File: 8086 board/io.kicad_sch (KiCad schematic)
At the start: 108 parts, among them SW1 SW_Push, SW10 SW_Push, SW11 SW_Push, SW12 SW_Push, SW13 SW_Push, SW14 SW_Push, SW15 SW_Push, SW16 SW_Push, SW17 SW_Push, SW18 SW_Push, SW19 SW_Push, SW2 SW_Push, SW20 SW_Push, SW21 SW_Push, SW22 SW_Push, SW23 SW_Push, SW24 SW_Push, SW25 SW_Push, SW26 SW_Push, SW27 SW_Push, SW28 SW_Push, SW29 SW_Push, SW3 SW_Push, SW30 SW_Push, SW31 SW_Push, SW32 SW_Push, SW4 SW_Push, SW5 SW_Push, SW6 SW_Push, SW7 SW_Push, SW8 SW_Push, SW9 SW_Push, U16 74AC373, U28 74AC373, U30 74AC00, U31 74HC02, U32 74AC373, U33 74AC373, U34 74AC373, U35 74AC373, U36 74AC373, U37 74AC373

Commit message: refactoring schematic files and structure
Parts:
- added U15: AMS1117-3.3, Package_TO_SOT_SMD:SOT-223-3_TabPin2, symbol Regulator_Linear:AMS1117-3.3
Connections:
- net +5V: now also U15.3 (VI)
- net GND: now also U15.1 (GND)
- new net +3.3V: U15.2 (VO)

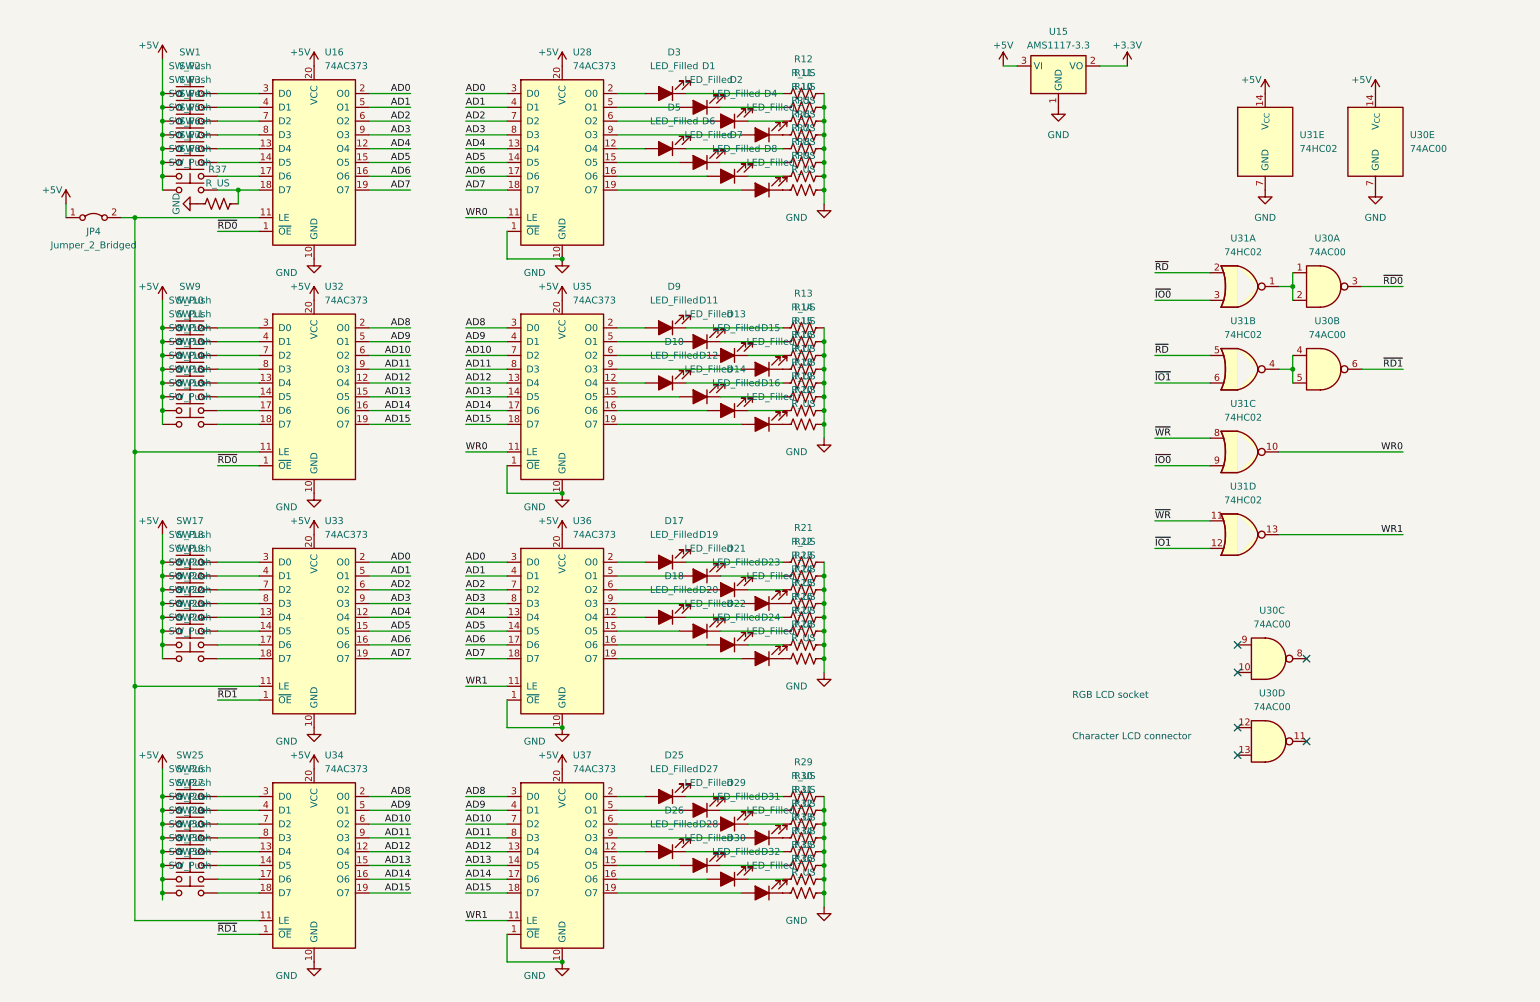
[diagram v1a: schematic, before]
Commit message: better schematic. initial pcb layout
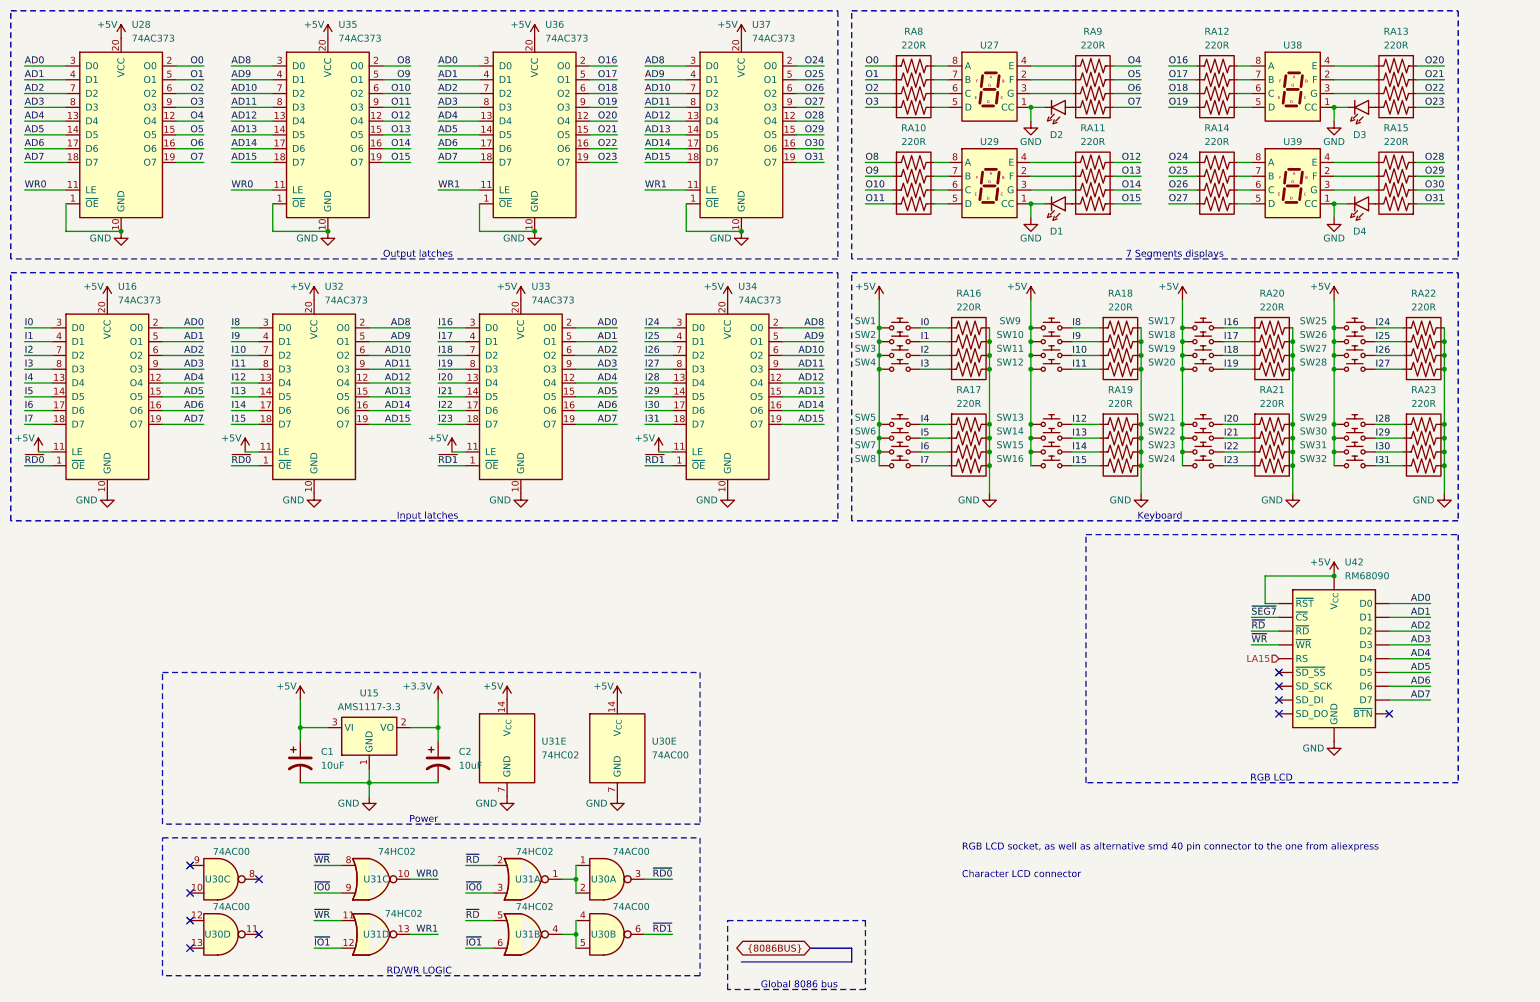
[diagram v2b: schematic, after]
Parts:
- removed D1, D10, D11, D12, D13, D14, D15, D16, D17, D18, D19, D2, D20, D21, D22, D23, D24, D25, D26, D27, D28, D29, D3, D30, D31, D32, D4, D5, D6, D7, D8, D9: LED_Filled, LED_SMD:LED_0603_1608Metric_Pad1.05x0.95mm_HandSolder, symbol Device:LED_Filled
- removed JP4: Jumper_2_Bridged, symbol Jumper:Jumper_2_Bridged
- removed R10, R11, R12, R13, R14, R15, R16, R17, R18, R19, R20, R21, R22, R23, R24, R25, R26, R27, R28, R29, R30, R31, R32, R33, R34, R35, R36, R37, R5, R6, R7, R8, R9: R_US, Resistor_SMD:R_0603_1608Metric_Pad0.98x0.95mm_HandSolder, symbol Device:R_US
- removed SW1, SW10, SW11, SW12, SW13, SW14, SW15, SW16, SW17, SW18, SW19, SW2, SW20, SW21, SW22, SW23, SW24, SW25, SW26, SW27, SW28, SW29, SW3, SW30, SW31, SW32, SW4, SW5, SW6, SW7, SW8, SW9: SW_Push, Button_Switch_SMD:SW_Push_1P1T_NO_6x6mm_H9.5mm, symbol Switch:SW_Push
- added C1, C2: 10uF, symbol Device:C_Polarized_US
- added D1, D2, D3, D4: LED, symbol 8086PC:LED
- added RA10, RA11, RA12, RA13, RA14, RA15, RA16, RA17, RA18, RA19, RA20, RA21, RA22, RA23, RA8, RA9: 220R, Resistor_SMD:R_Array_Concave_4x0603, symbol 8086PC:R_Array_4
- added SW1, SW10, SW11, SW12, SW13, SW14, SW15, SW16, SW17, SW18, SW19, SW2, SW20, SW21, SW22, SW23, SW24, SW25, SW26, SW27, SW28, SW29, SW3, SW30, SW31, SW32, SW4, SW5, SW6, SW7, SW8, SW9: ~, Button_Switch_SMD:SW_Push_1P1T_NO_6x6mm_H9.5mm, symbol 8086PC:SW_Push
- added U27, U29, U38, U39: ~, symbol 8086PC:2181AS
- added U42: RM68090, symbol 8086PC:RM68090
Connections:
- net +3.3V: now also C2.1
- net +5V: now also U16.11 (LE), U32.11 (LE), U33.11 (LE), U34.11 (LE), C1.1, SW1.1, SW10.1, SW11.1, SW12.1, SW13.1, SW14.1, SW15.1, SW16.1, SW17.1, SW18.1, SW19.1, SW2.1, SW20.1, SW21.1, SW22.1, SW23.1, SW24.1, SW25.1, SW26.1, SW27.1, SW28.1, SW29.1, SW3.1, SW30.1, SW31.1, SW32.1, SW4.1, SW5.1, SW6.1, SW7.1, SW8.1, SW9.1, U42. (~{WR})
- net AD0: now also U42. (~{WR})
- net AD1: now also U42. (~{WR})
- net AD2: now also U42. (~{WR})
- net AD3: now also U42. (~{WR})
- net AD4: now also U42. (~{WR})
- net AD5: now also U42. (~{WR})
- net AD6: now also U42. (~{WR})
- net AD7: now also U42. (~{WR})
- net GND: now also C1.2, C2.2, D1.2 (K), D2.2 (K), D3.2 (K), D4.2 (K), RA16.5, RA16.6, RA16.7, RA16.8, RA17.5, RA17.6, RA17.7, RA17.8, RA18.5, RA18.6, RA18.7, RA18.8, RA19.5, RA19.6, RA19.7, RA19.8, RA20.5, RA20.6, RA20.7, RA20.8, RA21.5, RA21.6, RA21.7, RA21.8, RA22.5, RA22.6, RA22.7, RA22.8, RA23.5, RA23.6, RA23.7, RA23.8, U27.1 (CC), U29.1 (CC), U38.1 (CC), U39.1 (CC), U42. (~{WR})
- net ~{RD}: now also U42. (~{WR})
- net ~{WR}: now also U42. (~{WR})
- net I12: now reaches U32.13 (D4)
- net I12: now also RA19.1, SW13.2
- net I13: now reaches U32.14 (D5)
- net I13: now also RA19.2, SW14.2
- net I14: now reaches U32.17 (D6)
- net I14: now also RA19.3, SW15.2
- net I15: now reaches U32.18 (D7)
- net I15: now also RA19.4, SW16.2
- net I8: now reaches U32.3 (D0)
- net I8: now also RA18.1, SW9.2
- net I9: now reaches U32.4 (D1)
- net I9: now also RA18.2, SW10.2
- net I10: now reaches U32.7 (D2)
- net I10: now also RA18.3, SW11.2
- net I11: now reaches U32.8 (D3)
- net I11: now also RA18.4, SW12.2
- net I23: now reaches U33.18 (D7)
- net I23: now also RA21.4, SW24.2
- net I16: now reaches U33.3 (D0)
- net I16: now also RA20.1, SW17.2
- net O4: now reaches U28.12 (O4)
- net O4: now also RA9.4
- net O19: now reaches U36.9 (O3)
- net O19: now also RA12.4
- net O3: now reaches U28.9 (O3)
- net O3: now also RA8.4
- net O27: now reaches U37.9 (O3)
- net O27: now also RA14.4
- net I24: now reaches U34.3 (D0)
- net I24: now also RA22.1, SW25.2
- net O0: now reaches U28.2 (O0)
- net O0: now also RA8.1
- net I26: now reaches U34.7 (D2)
- net I26: now also RA22.3, SW27.2
- net O25: now reaches U37.5 (O1)
- net O25: now also RA14.2
- net O12: now reaches U35.12 (O4)
- net O12: now also RA11.4
- net O13: now reaches U35.15 (O5)
- net O13: now also RA11.3
- net O14: now reaches U35.16 (O6)
- net O14: now also RA11.2
- net O15: now reaches U35.19 (O7)
- net O15: now also RA11.1
- net O8: now reaches U35.2 (O0)
- net O8: now also RA10.1
- net O9: now reaches U35.5 (O1)
- net O9: now also RA10.2
- net O10: now reaches U35.6 (O2)
- net O10: now also RA10.3
- net O11: now reaches U35.9 (O3)
- net O11: now also RA10.4
- net O17: now reaches U36.5 (O1)
- net O17: now also RA12.2
- net I4: now reaches U16.13 (D4)
- net I4: now also RA17.1, SW5.2
- net I1: now reaches U16.4 (D1)
- net I1: now also RA16.2, SW2.2
- net O21: now reaches U36.15 (O5)
- net O21: now also RA13.3
- net I30: now reaches U34.17 (D6)
- net I30: now also RA23.3, SW31.2
- net O6: now reaches U28.16 (O6)
- net O6: now also RA9.2
- net O30: now reaches U37.16 (O6)
- net O30: now also RA15.2
- net I5: now reaches U16.14 (D5)
- net I5: now also RA17.2, SW6.2
- net I19: now reaches U33.8 (D3)
- net I19: now also RA20.4, SW20.2
- net I6: now reaches U16.17 (D6)
- net I6: now also RA17.3, SW7.2
- net O28: now reaches U37.12 (O4)
- net O28: now also RA15.4
- net I7: now reaches U16.18 (D7)
- net I7: now also RA17.4, SW8.2
- net I28: now reaches U34.13 (D4)
- net I28: now also RA23.1, SW29.2
- net I29: now reaches U34.14 (D5)
- net I29: now also RA23.2, SW30.2
- net I31: now reaches U34.18 (D7)
- net I31: now also RA23.4, SW32.2
- net I25: now reaches U34.4 (D1)
- net I25: now also RA22.2, SW26.2
- net I27: now reaches U34.8 (D3)
- net I27: now also RA22.4, SW28.2
- net I22: now reaches U33.17 (D6)
- net I22: now also RA21.3, SW23.2
- net O24: now reaches U37.2 (O0)
- net O24: now also RA14.1
- net O5: now reaches U28.15 (O5)
- net O5: now also RA9.3
- net O7: now reaches U28.19 (O7)
- net O7: now also RA9.1
- net O1: now reaches U28.5 (O1)
- net O1: now also RA8.2
- net O2: now reaches U28.6 (O2)
- net O2: now also RA8.3
- net O16: now reaches U36.2 (O0)
- net O16: now also RA12.1
- net O22: now reaches U36.16 (O6)
- net O22: now also RA13.2
- net I17: now reaches U33.4 (D1)
- net I17: now also RA20.2, SW18.2
- net O29: now reaches U37.15 (O5)
- net O29: now also RA15.3
- net I2: now reaches U16.7 (D2)
- net I2: now also RA16.3, SW3.2
- net O31: now reaches U37.19 (O7)
- net O31: now also RA15.1
- net I20: now reaches U33.13 (D4)
- net I20: now also RA21.1, SW21.2
- net I3: now reaches U16.8 (D3)
- net I3: now also RA16.4, SW4.2
- net I21: now reaches U33.14 (D5)
- net I21: now also RA21.2, SW22.2
- net I18: now reaches U33.7 (D2)
- net I18: now also RA20.3, SW19.2
- net O20: now reaches U36.12 (O4)
- net O20: now also RA13.4
- net O18: now reaches U36.6 (O2)
- net O18: now also RA12.3
- net O23: now reaches U36.19 (O7)
- net O23: now also RA13.1
- net I0: now reaches U16.3 (D0)
- net I0: now also RA16.1, SW1.2
- net O26: now reaches U37.6 (O2)
- net O26: now also RA14.3
- new net: RA10.5, U29.5 (D)
- new net: RA10.6, U29.6 (C)
- new net: RA10.7, U29.7 (B)
- new net: RA10.8, U29.8 (A)
- new net: RA11.5, U29.4 (E)
- new net: RA11.6, U29.2 (F)
- new net: RA11.7, U29.3 (G)
- new net: D1.1 (A), RA11.8
- new net: RA9.6, U27.2 (F)
- new net: RA9.7, U27.3 (G)
- new net: RA9.5, U27.4 (E)
- new net: RA8.5, U27.5 (D)
- new net: RA8.6, U27.6 (C)
- new net: RA8.7, U27.7 (B)
- new net: RA8.8, U27.8 (A)
- new net: RA12.5, U38.5 (D)
- new net: RA12.6, U38.6 (C)
- new net: RA12.7, U38.7 (B)
- new net: RA12.8, U38.8 (A)
- new net: RA14.5, U39.5 (D)
- new net: RA14.6, U39.6 (C)
- new net: RA14.7, U39.7 (B)
- new net: RA14.8, U39.8 (A)
- new net: D3.1 (A), RA13.8
- new net: D4.1 (A), RA15.8
- new net: D2.1 (A), RA9.8
- new net: RA15.6, U39.2 (F)
- new net: RA15.7, U39.3 (G)
- new net: RA15.5, U39.4 (E)
- new net: RA13.6, U38.2 (F)
- new net: RA13.7, U38.3 (G)
- new net: RA13.5, U38.4 (E)
- new net LA15: U42. (~{WR})
- new net ~{SEG7}: U42. (~{WR})
- no-connect marks 6 -> 11
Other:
- note added: "7 Segments displays"
- note added: "Global 8086 bus"
- note added: "Input latches"
- note added: "Keyboard"
- note added: "Output latches"
- note added: "Power"
- note added: "RD/WR LOGIC"
- note added: "RGB LCD"
- note added: "RGB LCD socket, as well as alternative smd 40 pin connector to the one from aliexpress"
- note removed: "RGB LCD socket"
- moved on the sheet: U15, U16, U28, U30A, U30B, U30C, U30D, U30E, U31A, U31B, U31C, U31D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

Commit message: Schematic finished! (some footprint assignments are still needed)
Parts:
- removed C1, C2: 10uF, symbol Device:C_Polarized_US
- removed U15: AMS1117-3.3, Package_TO_SOT_SMD:SOT-223-3_TabPin2, symbol Regulator_Linear:AMS1117-3.3
- removed U30: 74AC00, Package_SO:SOIC-14_3.9x8.7mm_P1.27mm, symbol 8086PC:74AC00
- removed unit 5 of U31
- added J3: RGB LCD, 8086PC:FPC_40, symbol 8086PC:LCD_RGB_40P
- added JP?: LCD RST, Jumper:SolderJumper-3_P2.0mm_Open_TrianglePad1.0x1.5mm, symbol 8086PC:SolderJumper
- added JP?: Width, Jumper:SolderJumper-3_P2.0mm_Open_TrianglePad1.0x1.5mm, symbol 8086PC:SolderJumper
- added JP?: D/~{C}, Jumper:SolderJumper-3_P2.0mm_Open_TrianglePad1.0x1.5mm, symbol 8086PC:SolderJumper
- added R? (x3): 100R, Resistor_SMD:R_0603_1608Metric_Pad0.98x0.95mm_HandSolder, symbol 8086PC:R
- added U? (x2): 74HC02, Package_SO:SOIC-14_3.9x8.7mm_P1.27mm, symbol 8086PC:74HC02
- D25: renamed from D2; footprint (none) -> LED_SMD:LED_0603_1608Metric_Pad1.05x0.95mm_HandSolder
- D26: renamed from D1; footprint (none) -> LED_SMD:LED_0603_1608Metric_Pad1.05x0.95mm_HandSolder
- D27: renamed from D3; footprint (none) -> LED_SMD:LED_0603_1608Metric_Pad1.05x0.95mm_HandSolder
- D28: renamed from D4; footprint (none) -> LED_SMD:LED_0603_1608Metric_Pad1.05x0.95mm_HandSolder
- DS1: renamed from U27; value ~ -> 7SEG
- DS2: renamed from U29; value ~ -> 7SEG
- DS3: renamed from U38; value ~ -> 7SEG
- DS4: renamed from U39; value ~ -> 7SEG
- J2: renamed from U42; footprint (none) -> 8086PC:RM68090 RGB LCD module
- SW1, SW10, SW11, SW12, SW13, SW14, SW15, SW16, SW17, SW18, SW19, SW2, SW20, SW21, SW22, SW23, SW24, SW25, SW26, SW27, SW28, SW29, SW3, SW30, SW31, SW32, SW4, SW5, SW6, SW7, SW8, SW9: footprint Button_Switch_SMD:SW_Push_1P1T_NO_6x6mm_H9.5mm -> 8086PC:SW_Push_1P1T_NO_6x6mm_H9.5mm
- U29: renamed from U34; footprint Package_SO:SOIC-20W_7.5x12.8mm_P1.27mm -> Package_SO:TSSOP-20_4.4x6.5mm_P0.65mm
- renumbered U28 to U22, U35 to U23, U36 to U24, U37 to U25, U16 to U26, U32 to U27, U33 to U28, U31 to U4, U31 to U5
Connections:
- net +3.3V: now also J2.2 (V_{CC}), J3.6 (VDDI), J3.7 (VDDA), JP?.2, JP?.2
- net +5V: now also J3.33 (A); no longer J2. (~{WR})
- net AD0: now also J2.21 (D0), J3.17 (DB0); no longer J2. (~{WR})
- net AD1: now also J2.22 (D1), J3.18 (DB1); no longer J2. (~{WR})
- net AD10: now also J3.27 (DB10)
- net AD11: now also J3.28 (DB11)
- net AD12: now also J3.29 (DB12)
- net AD13: now also J3.30 (DB13)
- net AD14: now also J3.31 (DB14)
- net AD15: now also J3.32 (DB15)
- net AD2: now also J2.15 (D2), J3.19 (DB2); no longer J2. (~{WR})
- net AD3: now also J2.16 (D3), J3.20 (DB3); no longer J2. (~{WR})
- net AD4: now also J2.17 (D4), J3.21 (DB4); no longer J2. (~{WR})
- net AD5: now also J2.18 (D5), J3.22 (DB5); no longer J2. (~{WR})
- net AD6: now also J2.19 (D6), J3.23 (DB6); no longer J2. (~{WR})
- net AD7: now also J2.20 (D7), J3.24 (DB7); no longer J2. (~{WR})
- net AD8: now also J3.25 (DB8)
- net AD9: now also J3.26 (DB9)
- net GND: now also J2.5 (GND), J3.16 (GND), J3.37 (GND), J3.39 (IM1), J3.40 (IM2), J3.5 (GND), JP?.1, R?.1, R?.1, R?.1; no longer J2. (~{WR})
- net LA15: now also JP?.1; no longer J2. (~{WR})
- net O15: now also JP?.2
- net O7: now also JP?.1
- net WR0: now also U4.4; no longer U4.10
- net WR1: now also U4.10; no longer U5.13
- net ~{IO0}: now also U4.6; no longer U4.9
- net ~{IO1}: now also U4.9, U?.9; no longer U4.6, U5.12
- net ~{RD0}: now also U?.4
- net ~{RD1}: now also U5.13
- net ~{RD}: now also J2.7 (~{RD}), J3.12 (~{RD}), U?.8; no longer J2. (~{WR}), U4.5
- net ~{SEG7}: now also J2.10 (~{CS}), J3.9 (~{CS}); no longer J2. (~{WR})
- net ~{WR}: now also J2.8 (~{WR}), U4.5, J3.11 (~{WR}); no longer J2. (~{WR}), U5.11
- net at U5.1: now also U?.5, U?.6
- new net: U5.11, U5.12, U?.10
- new net: J3.36 (K), R?.2
- new net: J3.35 (K), R?.2
- new net: J3.34 (K), R?.2
- new net D/~{C}: J2.9 (RS), J3.10 (D/~{C}), JP?.3
- new net IM0: J3.38 (IM0), JP?.3
- new net ~{LCD_RST}: J2.11 (~{RST}), J3.15 (~{RESET}), JP?.3
- no-connect marks 11 -> 12
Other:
- note added: "40-Pin RGB LCD"
- note added: "IN[0-7]"
- note added: "IN[16-23]"
- note added: "IN[24-31]"
- note added: "IN[8-15]"
- note added: "Jumpers"
- note added: "OUT[0-7]"
- note added: "OUT[16-23]"
- note added: "OUT[24-31]"
- note added: "OUT[8-15]"
- note added: "RGB LCD module"
- note removed: "Character LCD connector"
- note removed: "Power"
- note removed: "RGB LCD"
- note removed: "RGB LCD socket, as well as alternative smd 40 pin connector to the one from aliexpress"
- moved on the sheet: U4B, U4C, U5A, U5D
